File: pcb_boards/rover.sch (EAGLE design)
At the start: 16 parts, among them IC1 MC33269ST-5.0T3, J1 B02B-PASK(LF)(SN)

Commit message: finished pcb, added BOM
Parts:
- removed J1: B02B-PASK(LF)(SN), Headers:B02B-PASK(LF)(SN)
- added ESC, PWR_IN, SERVO: JST-XH-02-PIN-LONG-PAD, Rembrandt Electronics - JST XH Connectors v1-0:JST-XH-02-PIN-LONG-PAD
- added RECIEVER: JST-XH-03-PIN-LONG-PAD, Rembrandt Electronics - JST XH Connectors v1-0:JST-XH-03-PIN-LONG-PAD
- C1, C2, D1, GREEN, IC1, JP3, JP4, R1, S1, U$5: OC_NEWARK (none) -> unknown
- FL_ENC, FR_ENC, RL_ENC, RR_ENC: value B4B-XH-A(LF)(SN) -> JST-XH-04-PIN-LONG-PAD; device Headers:B4B-XH-A(LF)(SN) -> Rembrandt Electronics - JST XH Connectors v1-0:JST-XH-04-PIN-LONG-PAD
- STEER_ENC: value B3B-ZR(LF)(SN) -> JST-XH-03-PIN-LONG-PAD; device Headers:B3B-ZR(LF)(SN) -> Rembrandt Electronics - JST XH Connectors v1-0:JST-XH-03-PIN-LONG-PAD
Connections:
- net +5V: now also FL_ENC-1.S, FR_ENC-1.S, RL_ENC-1.S, RR_ENC-1.S, STEER_ENC-1.S; no longer FL_ENC.1, FR_ENC.1, RL_ENC.1, RR_ENC.1, STEER_ENC.1
- net ESC: now also ESC-1.S
- net FL_ENC_A: now also FL_ENC-2.S; no longer FL_ENC.2
- net FL_ENC_B: now also FL_ENC-4.S; no longer FL_ENC.4
- net FR_ENC_A: now also FR_ENC-2.S; no longer FR_ENC.2
- net FR_ENC_B: now also FR_ENC-4.S; no longer FR_ENC.4
- net GND: now also ESC-2.S, FL_ENC-3.S, FR_ENC-3.S, GREEN.C, PWR_IN-2.S, RECIEVER-3.S, RL_ENC-3.S, RR_ENC-3.S, SERVO-2.S, STEER_ENC-3.S; no longer FL_ENC.3, FR_ENC.3, J1.2, RL_ENC.3, RR_ENC.3, STEER_ENC.3
- net PWRIN: now also PWR_IN-1.S; no longer J1.1
- net REC_ESC: now also RECIEVER-1.S
- net REC_SERVO: now also RECIEVER-2.S
- net RL_ENC_A: now also RL_ENC-2.S; no longer RL_ENC.2
- net RL_ENC_B: now also RL_ENC-4.S; no longer RL_ENC.4
- net RR_ENC_A: now also RR_ENC-2.S; no longer RR_ENC.2
- net RR_ENC_B: now also RR_ENC-4.S; no longer RR_ENC.4
- net SERVO: now also SERVO-1.S
- net STEER_ENC: now also STEER_ENC-2.S; no longer STEER_ENC.2
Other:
- note added: "Debug"
- note added: "Designed by Alborz Jelvani"
- note added: "I/O Ports"
- note added: "IMU"
- note added: "Microcontroller"
- note added: "Power Managment"
- note added: "Rutgers University"
- note added: "Schematic for PCB on ruRover. The PCB has the function of being the low level hardware controller and interface. It communicates with a Linux computer over serial from the microcontroller. Input voltage is to be 12V."
- moved on the sheet: GREEN, JP3, JP4, R1

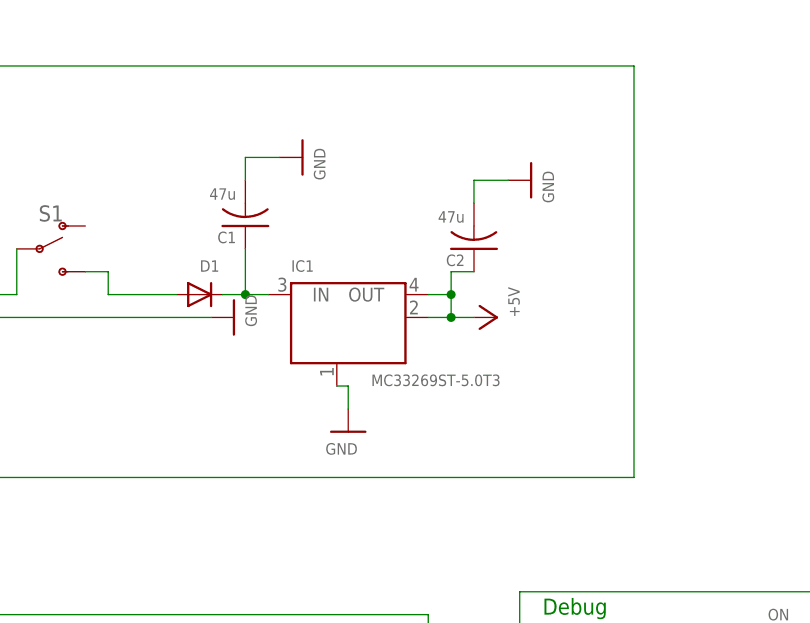
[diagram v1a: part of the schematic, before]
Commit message: changed LDO regulator to active one in stock
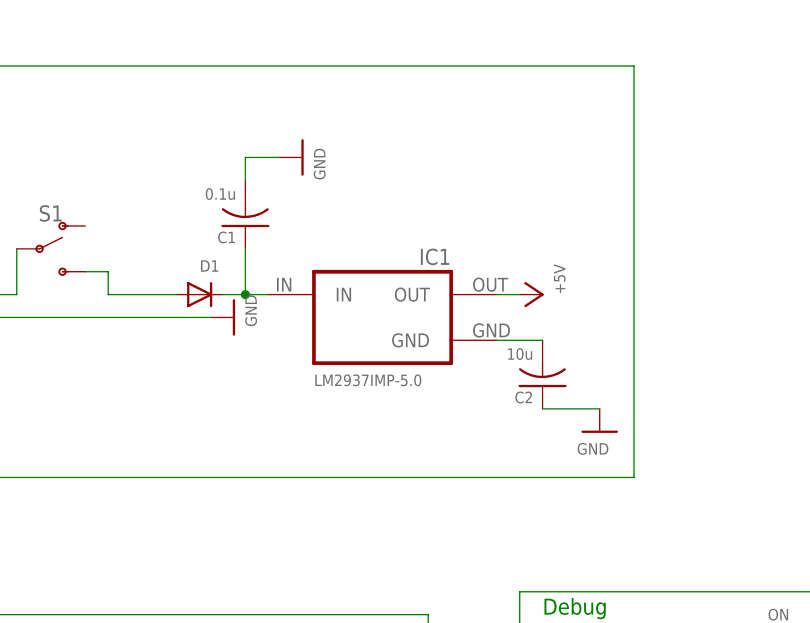
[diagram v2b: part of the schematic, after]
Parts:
- C1: value 47u -> 0.1u
- C2: value 47u -> 10u
- IC1: value MC33269ST-5.0T3 -> LM2937IMP-5.0; device linear:MC33269ST-3.3T3 -> lm2937:LM2937IMP-5.0; OC_NEWARK unknown -> (none)
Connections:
- new net N$9: C2.2, IC1G$1.GND
- net +5V: now also IC1G$1.OUT; no longer C2.1, IC1.OUT, IC1.OUT@1
- net GND: now also C2.1; no longer C2.2, IC1.GND/ADJ
- net N$2: now also IC1G$1.IN; no longer IC1.IN
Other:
- moved on the sheet: C2
